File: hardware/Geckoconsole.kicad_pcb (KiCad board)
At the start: 2 copper layers, 69.1 x 42.4 mm, 59 parts, among them J1 Conn_01x08_Male, J31 Conn_01x07_Female, J50 USB-C, J70 I²C, J71 I²C, J81 Conn_01x07, Q51 S8050, Q52 S8050, SW2 Reset, SW41 Rotary_Encoder_Switch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

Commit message: Console PCB: Fix missing VCC connection on rotary enc
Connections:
- R41 pad 2: Net-(R41-Pad2) -> +3V3
- R42 pad 2: Net-(R41-Pad2) -> +3V3
- R43 pad 2: Net-(R41-Pad2) -> +3V3
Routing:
- net +3V3: track 69.3 -> 90.8 mm
- net Net-(R41-Pad2): track 9.94 -> 0.00 mm

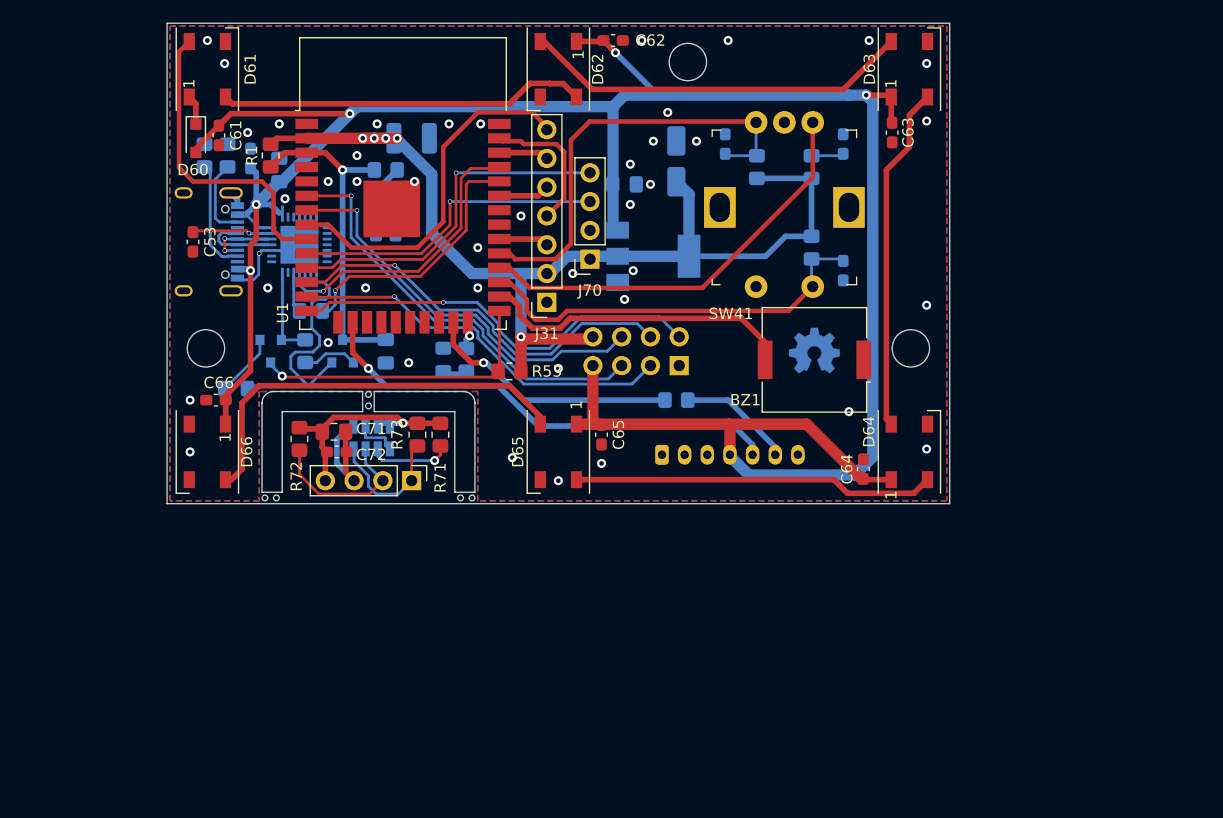
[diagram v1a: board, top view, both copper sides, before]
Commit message: Hardware Console: Start with HW Revision 2
* include 2nd navigation button
* move USB-C interface onto separate daughter board
* hide VCNL4040 parts from PCB
* turn ESP32 180°
* move LCD pin header to top of board
* switch a few GPIOs
* place parts on PCB
* TBD: Routing
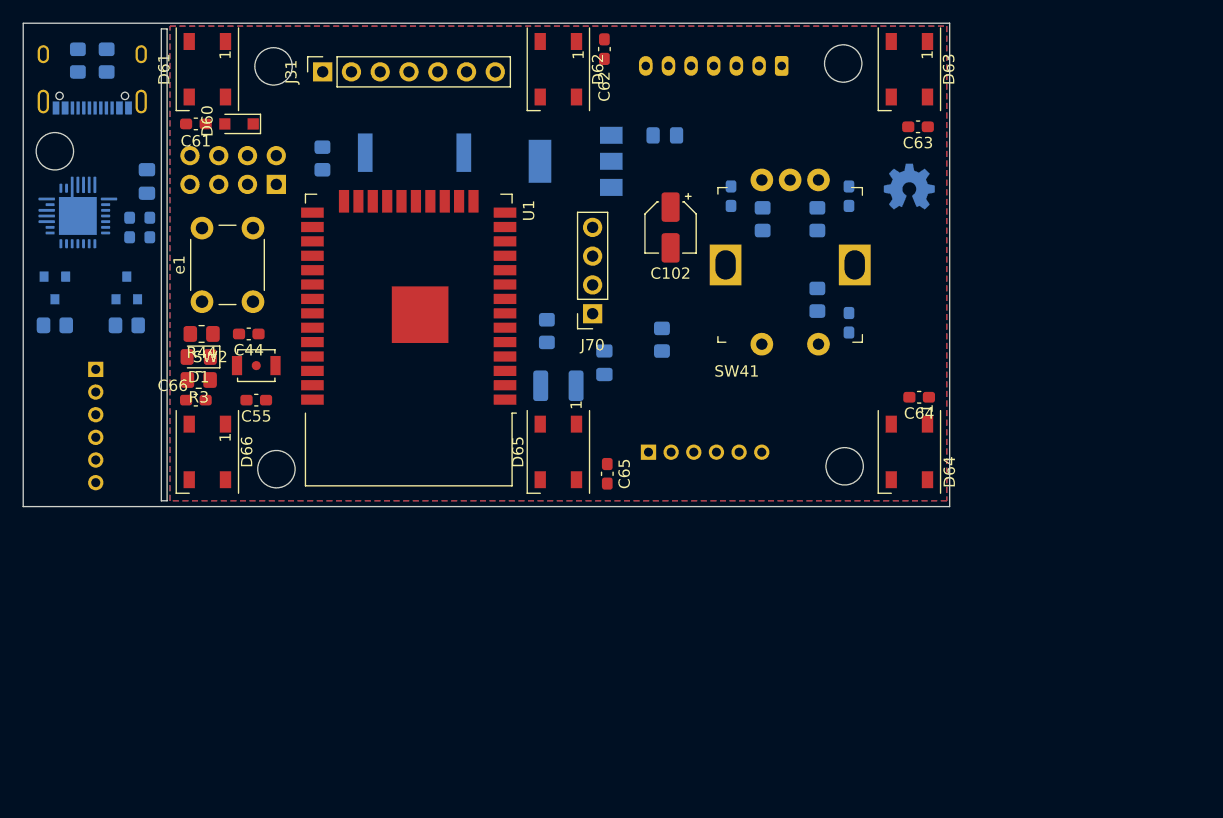
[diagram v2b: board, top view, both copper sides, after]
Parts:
- removed C71: 100nF, Capacitor_SMD:C_0603_1608Metric_Pad1.08x0.95mm_HandSolder
- removed C72: 2.2µF, Capacitor_SMD:C_0805_2012Metric_Pad1.18x1.45mm_HandSolder
- removed J71: I²C, Connector_PinHeader_2.54mm:PinHeader_1x04_P2.54mm_Vertical
- removed R50, R81: 470R, Resistor_SMD:R_0805_2012Metric_Pad1.20x1.40mm_HandSolder
- removed the R55 at (69.8, 48.3)
- removed R71, R72: 4k7, Resistor_SMD:R_0805_2012Metric_Pad1.20x1.40mm_HandSolder
- removed R73: 12k, Resistor_SMD:R_0805_2012Metric_Pad1.20x1.40mm_HandSolder
- removed U70: VCNL4040M3OE, Fraxinas:VISHAY_VCNL4040_4X2X1.1
- added C44: 10nF, Capacitor_SMD:C_0603_1608Metric_Pad1.08x0.95mm_HandSolder, F.Cu at (57.8, 62.7)
- added J11: Conn_01x06_Male, Connector_PinSocket_2.00mm:PinSocket_1x06_P2.00mm_Horizontal, B.Cu at (93.0, 73.2)
- added J51: Conn_01x06_Male, Connector_PinHeader_2.00mm:PinHeader_1x06_P2.00mm_Horizontal, B.Cu at (44.2, 65.9)
- added R44: 68k, Resistor_SMD:R_0805_2012Metric_Pad1.20x1.40mm_HandSolder, F.Cu at (53.6, 62.7)
- added R54: 470R, Resistor_SMD:R_0805_2012Metric_Pad1.20x1.40mm_HandSolder, B.Cu at (94.2, 63.2)
- added e1: Button2, Button_Switch_THT:SW_PUSH_6mm_H5mm, F.Cu at (53.6, 59.9)
- BZ1, C53, R1, R53: moved to B.Cu
- C102, C55, D1, R3, SW2: moved to F.Cu
- moved BZ1 39.8 mm to (72.4, 46.7), turned to 0 degrees
- moved J1 39.0 mm to (60.2, 49.5)
- moved J81 35.9 mm to (104.8, 39.1), turned to 180 degrees
- moved R1 28.9 mm to (84.1, 62.5)
- moved J31 28.4 mm to (64.3, 39.6), turned to 90 degrees
- moved C2 25.4 mm to (85.1, 67.3)
- moved R53 25.0 mm to (64.3, 47.2), turned to -90 degrees
- moved R3 23.7 mm to (53.3, 66.8), turned to 180 degrees
- moved D1 21.6 mm to (53.3, 64.8), turned to 180 degrees
- moved Q52 19.9 mm to (47.0, 58.7)
- moved Q51 19.9 mm to (40.6, 58.7)
- moved U2 19.7 mm to (42.7, 52.3), turned to -90 degrees
- moved C1 19.3 mm to (89.2, 65.3)
- moved SW2 18.7 mm to (58.4, 65.5), turned to 0 degrees
- moved C55 18.4 mm to (58.4, 68.6), turned to 180 degrees
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- renumbered R57 to R55
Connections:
- C43 pad 2: GND -> Net-(C43-Pad2)
- C55 pad 1: /Reset_switch -> EN
- J81 pad 6: Net-(J81-Pad6) -> RX1
- Q51 pad 2: /DTR -> /RTS
- Q51 pad 3: IO0 -> EN
- Q52 pad 2: /RTS -> /DTR
- Q52 pad 3: EN -> IO0
- R51 pad 2: /RTS -> /DTR
- R52 pad 2: /DTR -> /RTS
- SW2 pad 2: /Reset_switch -> EN
- SW41 pad S2: GND -> Net-(C43-Pad2)
- U1 pad 6: GPIO34 -> BUTTON2
- U2 pad 25: TXD0 -> RXD
- U2 pad 26: /TXD -> TXD
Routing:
- net +5V: track 216.6 -> 0.00 mm, vias 5 -> 0
- net +3V3: track 90.8 -> 0.00 mm, vias 5 -> 0
- net ENC_A: track 43.2 -> 0.00 mm
- net TX1: track 42.2 -> 0.00 mm, vias 1 -> 0
- net ENC_B: track 39.1 -> 0.00 mm
- net GPIO34: track 37.5 -> 0.00 mm, vias 1 -> 0
- net GPIO12: track 37.1 -> 0.00 mm, vias 1 -> 0
- net Net-(D65-Pad2): track 36.4 -> 0.00 mm
- net ENC_SW: track 36.2 -> 0.00 mm
- net GPIO27: track 36.1 -> 0.00 mm, vias 1 -> 0
- net GPIO35: track 35.8 -> 0.00 mm, vias 1 -> 0
- net GPIO14: track 34.6 -> 0.00 mm, vias 1 -> 0
- net Net-(D62-Pad2): track 34.5 -> 0.00 mm
- net Net-(D61-Pad2): track 32.5 -> 0.00 mm
- net Net-(D64-Pad2): track 32.0 -> 0.00 mm
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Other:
- board size 69.1 x 42.4 mm -> 81.8 x 42.7 mm

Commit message: Hardware Console: Route USB daughter board & some more GPIO shuffling
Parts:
- removed C55: 100nF, Capacitor_SMD:C_0603_1608Metric_Pad1.08x0.95mm_HandSolder
- moved SW2 11.8 mm to (47.5, 70.1), turned to -90 degrees
- moved C53 7.38 mm to (47.8, 46.0), turned to 180 degrees
- moved Q52 5.88 mm to (41.2, 59.4), turned to -90 degrees
- moved R52 5.88 mm to (41.2, 62.7), turned to 0 degrees
- moved Q51 5.66 mm to (46.2, 59.4), turned to 90 degrees
- moved R51 5.66 mm to (46.2, 62.7), turned to 180 degrees
- moved C52 3.21 mm to (48.0, 56.4), turned to 0 degrees
- moved U2 1.70 mm to (44.2, 53.1), turned to -45 degrees
- moved C51 1.44 mm to (47.8, 48.3), turned to 0 degrees
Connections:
- BZ1 pad 1: GND -> Net-(BZ1-Pad1)
- BZ1 pad 2: Net-(BZ1-Pad2) -> GND
- J1 pad 2: GPIO12 -> GPIO02
- J1 pad 3: GPIO14 -> GPIO12
- J1 pad 4: GPIO27 -> GPIO15
- J1 pad 5: GPIO34 -> GPIO17
- J51 pad 4: EN -> EN'
- J51 pad 5: IO0 -> IO0'
- Q51 pad 3: EN -> EN'
- Q52 pad 3: IO0 -> IO0'
- R3 pad 2: Net-(R3-Pad2) -> GPIO02
- SW2 pad 2: EN -> EN'
- U1 pad 12: GPIO27 -> ENC_B
- U1 pad 13: GPIO14 -> ENC_A
- U1 pad 23: RX1 -> GPIO15
- U1 pad 24: Net-(R3-Pad2) -> GPIO02
- U1 pad 26: Net-(BZ1-Pad2) -> RGB
- U1 pad 27: ENC_SW -> Net-(BZ1-Pad1)
- U1 pad 28: ENC_A -> GPIO17
- U1 pad 29: ENC_B -> BUTTON2
- U1 pad 6: BUTTON2 -> ENC_SW
- U1 pad 9: RGB -> RX1
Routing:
- net +5V: track 0.00 -> 60.2 mm, vias 0 -> 4
- net EN': track 0.00 -> 17.5 mm
- net TXD: track 0.00 -> 17.2 mm, vias 0 -> 1
- net RXD: track 0.00 -> 15.3 mm, vias 0 -> 1
- net IO0': track 0.00 -> 14.7 mm
- net /D-: track 0.00 -> 14.0 mm
- net /D+: track 0.00 -> 12.5 mm, vias 0 -> 2
- net /DTR: track 0.00 -> 12.2 mm, vias 0 -> 2
- net /RTS: track 0.00 -> 9.59 mm
- net Net-(C53-Pad2): track 0.00 -> 7.30 mm
- net Net-(Q52-Pad1): track 0.00 -> 4.32 mm
- net Net-(J50-PadB5): track 0.00 -> 3.38 mm
- net Net-(J50-PadA5): track 0.00 -> 3.19 mm
- net Net-(Q51-Pad1): track 0.00 -> 2.32 mm
- net GND: track 0.00 -> 1.64 mm, vias 0 -> 9
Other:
- outline, holes or cut-outs redrawn
- board text added: "GND RXD TXD EN IO0 +5V"
- board text added: "Ver. 2.0 3/2022"
- board text removed: "Ver. 1.0 1/2022"

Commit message: Hardware Console: Route PCB, Pannelize
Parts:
- added G***: LOGO, Fraxinas:purplegecko, F.Cu at (93.0, 84.6)
- C1, C2, R1, R53: moved to F.Cu
- C102, C44, R44: moved to B.Cu
- D61, D62, D63, D64, D65, D66: footprint LED_SMD:LED_WS2812B_PLCC4_5.0x5.0mm_P3.2mm -> Fraxinas:LED_WS2812B_PLCC4_5.0x5.0mm_P3.2mm_Marking
- J1: value Conn_01x08_Male -> Conn_01x06_Male; footprint Connector_PinHeader_2.54mm:PinHeader_2x04_P2.54mm_Vertical -> Connector_PinHeader_2.54mm:PinHeader_2x03_P2.54mm_Vertical
- moved R53 69.1 mm to (117.9, 90.9)
- moved LOGO1 47.4 mm to (136.7, 93.5)
- moved R54 39.6 mm to (114.6, 97.3)
- moved C101 39.6 mm to (116.3, 78.2)
- moved R1 39.3 mm to (111.3, 90.9), turned to -90 degrees
- moved R44 38.5 mm to (78.7, 91.9), turned to 0 degrees
- moved C62 36.1 mm to (106.4, 69.3), turned to 0 degrees
- moved C1 36.1 mm to (114.6, 90.9), turned to 90 degrees
- moved J11 35.0 mm to (117.9, 97.8)
- moved C66 34.7 mm to (76.7, 94.0)
- moved R3 34.4 mm to (79.0, 89.7), turned to 90 degrees
- moved D66 33.9 mm to (76.2, 98.8)
- moved D65 33.9 mm to (107.2, 98.8)
- moved D64 33.9 mm to (138.2, 98.8)
- moved BZ1 33.8 mm to (96.3, 70.6)
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- renumbered SW2 to SW1, e1 to SW2
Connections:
- C61 pad 1: +5V -> Net-(C61-Pad1)
- D60 pad 1: Net-(D60-Pad1) -> Net-(C61-Pad1)
- D61 pad 1: Net-(D60-Pad1) -> Net-(C61-Pad1)
- J1 pad 2: GPIO02 -> GPIO12
- J1 pad 3: GPIO12 -> GPIO15
- J1 pad 4: GPIO15 -> GPIO17
- J1 pad 5: GPIO17 -> GPIO35
- J1 pad 6: GPIO35 -> +3V3
- R3 pad 2: GPIO02 -> Net-(R3-Pad2)
- U1 pad 12: ENC_B -> ENC_A
- U1 pad 13: ENC_A -> ENC_B
- U1 pad 24: GPIO02 -> Net-(R3-Pad2)
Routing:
- net +5V: track 60.2 -> 249.1 mm, vias 4 -> 5
- net +3V3: track 0.00 -> 139.7 mm, vias 0 -> 4
- net IO0: track 0.00 -> 56.5 mm, vias 0 -> 2
- net TXD0: track 0.00 -> 44.3 mm, vias 0 -> 1
- net ENC_SW: track 0.00 -> 41.3 mm
- net RX1: track 0.00 -> 37.7 mm, vias 0 -> 1
- net SPI_DC: track 0.00 -> 37.5 mm, vias 0 -> 1
- net ENC_A: track 0.00 -> 36.3 mm
- net RXD0: track 0.00 -> 35.8 mm, vias 0 -> 1
- net Net-(D63-Pad2): track 0.00 -> 34.8 mm
- net GPIO35: track 0.00 -> 34.2 mm, vias 0 -> 2
- net Net-(D65-Pad2): track 0.00 -> 33.4 mm
- net SPI_MOSI: track 0.00 -> 33.3 mm, vias 0 -> 1
- net TX1: track 0.00 -> 32.2 mm, vias 0 -> 1
- net Net-(D61-Pad2): track 0.00 -> 31.6 mm
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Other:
- board size 81.8 x 42.7 mm -> 83.7 x 43.2 mm
- board text added: "12 17 3V3"
- board text added: "3V3"
- board text added: "5V"
- board text added: "BL"
- board text added: "CLK"
- board text added: "DC"
- board text added: "GND"
- board text added: "GND 15 35"
- board text added: "I2C VCNL4040"
- board text added: "MH-Z19 CO2 Sensor"
- board text added: "MOSI"
- board text added: "RES"
- board text added: "SCK"
- board text added: "SDI"
- board text added: "ST7789V SPI Display"
- board text added: "►"
- board text added: "◄"
- board text removed: "Reset"

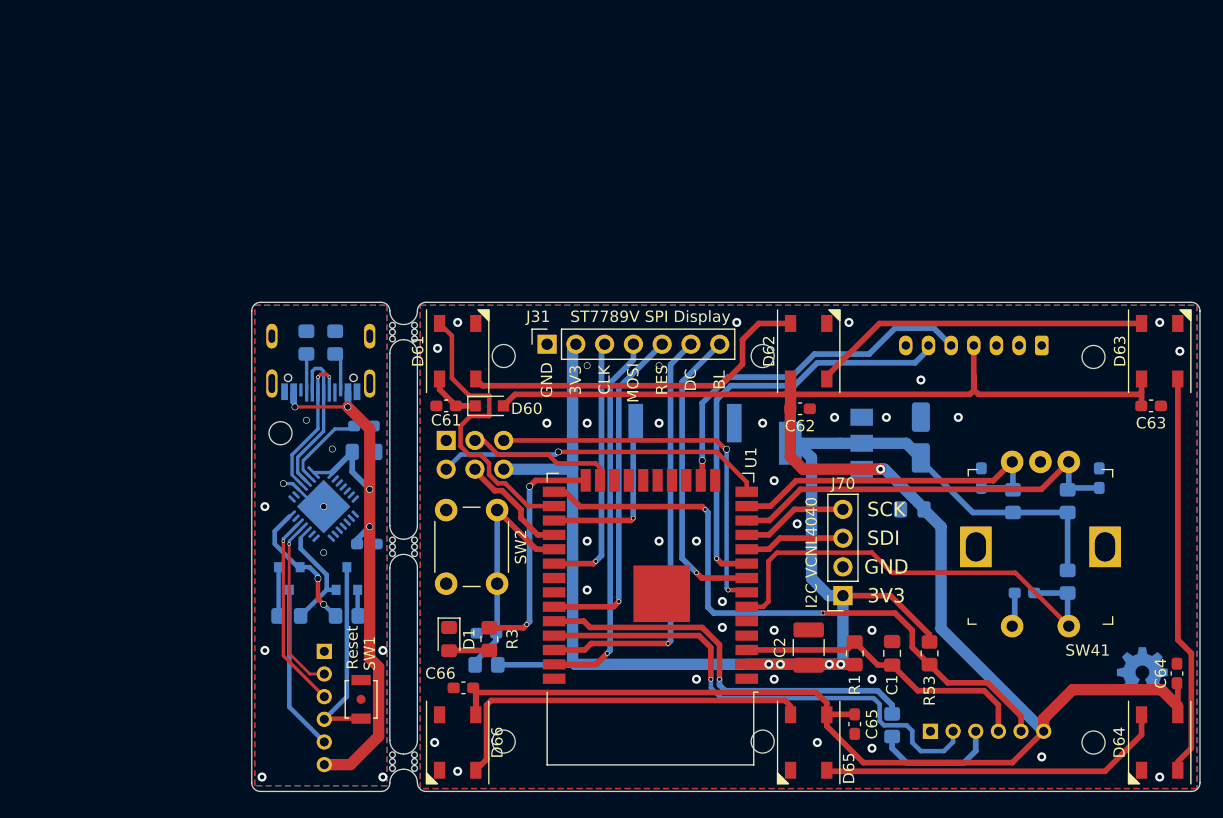
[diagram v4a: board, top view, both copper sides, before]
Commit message: Hardware Console: Improve Layout: DRC, Mouse Bites, placement, silkscreen
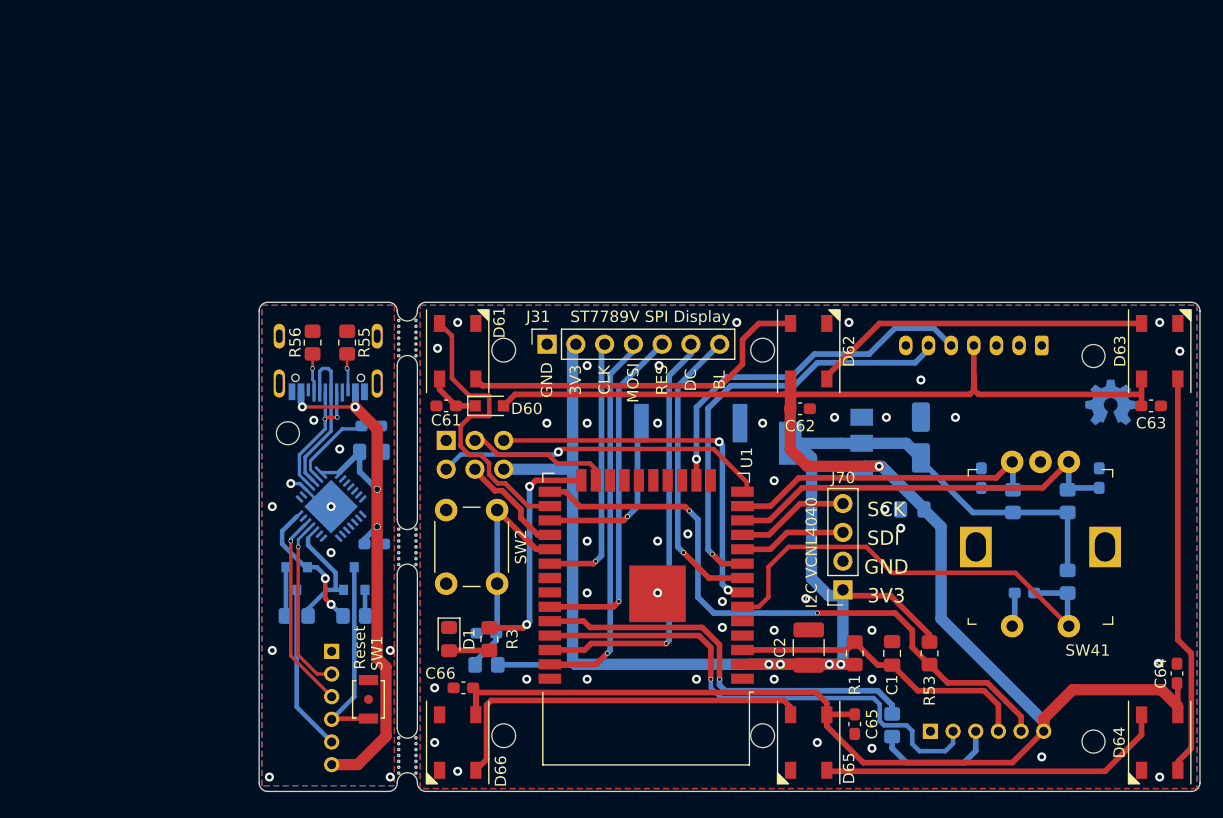
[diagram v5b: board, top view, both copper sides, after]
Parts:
- J11: value Conn_01x06_Male -> Conn_01x06_Female
- R55, R56: moved to F.Cu
- moved LOGO1 23.8 mm to (133.9, 69.8)
- moved G*** 2.01 mm to (94.1, 86.2)
- moved R55 1.05 mm to (66.4, 63.5)
- moved C51 0.65 mm to (68.6, 73.2)
- moved C52 0.65 mm to (68.8, 81.3)
- moved C53 0.65 mm to (68.6, 70.9)
- moved Q51 0.65 mm to (67.1, 84.3)
- moved R51 0.65 mm to (67.1, 87.6)
- moved U2 0.65 mm to (65.0, 78.0)
- moved Q52 0.65 mm to (62.0, 84.3)
- moved R52 0.65 mm to (62.0, 87.6)
- moved J50 0.65 mm to (64.8, 64.0)
- moved J51 0.65 mm to (65.1, 90.8)
- moved SW1 0.65 mm to (68.3, 95.0)
- moved R56 0.54 mm to (63.4, 63.5)
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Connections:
- C51 pad 1: +5V -> +5VP
- C51 pad 2: GND -> GNDD
- C52 pad 1: +5V -> +5VP
- C52 pad 2: GND -> GNDD
- C53 pad 1: GND -> GNDD
- J50 pad A1: GND -> GNDD
- J50 pad A12: GND -> GNDD
- J50 pad A4: +5V -> +5VP
- J50 pad A9: +5V -> +5VP
- J50 pad B1: GND -> GNDD
- J50 pad B12: GND -> GNDD
- J50 pad B4: +5V -> +5VP
- J50 pad B9: +5V -> +5VP
- J50 pad S1: GND -> GNDD
- J51 pad 1: GND -> GNDD
- J51 pad 6: +5V -> +5VP
- R55 pad 1: GND -> GNDD
- R56 pad 1: GND -> GNDD
- SW1 pad 1: GND -> GNDD
- U2 pad 29: GND -> GNDD
- U2 pad 3: GND -> GNDD
- U2 pad 7: +5V -> +5VP
- U2 pad 8: +5V -> +5VP
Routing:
- net +5V: track 249.1 -> 188.4 mm, vias 5 -> 1
- net +5VP: track 0.00 -> 59.9 mm, vias 0 -> 4
- net GND: track 1.64 -> 0.00 mm, vias 45 -> 42
- net GNDD: track 0.00 -> 1.64 mm, vias 0 -> 10
- net IO0: track 56.5 -> 55.6 mm
- net +3V3: track 139.7 -> 138.8 mm
- net Net-(D65-Pad2): track 33.4 -> 34.1 mm
- net RX1: track 37.7 -> 38.4 mm
- net Net-(R3-Pad2): track 20.9 -> 20.5 mm, vias 3 -> 2
- net Net-(J50-PadA5): track 3.19 -> 3.46 mm, vias 0 -> 1
- net Net-(J50-PadB5): track 3.38 -> 3.21 mm, vias 0 -> 1
- added copper zone on B.Cu, net GNDD
- added copper zone on F.Cu, net GNDD
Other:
- board size 83.7 x 43.2 mm -> 83.1 x 43.2 mm
